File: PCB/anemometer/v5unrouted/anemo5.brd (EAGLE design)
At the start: 100 x 80 mm, 77 parts, among them IC1 AD8223, IC2 AD8223, IC3 AD8223, IC4 AD8223, IC5 TL072D, IC6 TL072D, IC7 TL072D, J1 RJ12STRAIGHT-I2C, J2 RJ12STRAIGHT-I2C

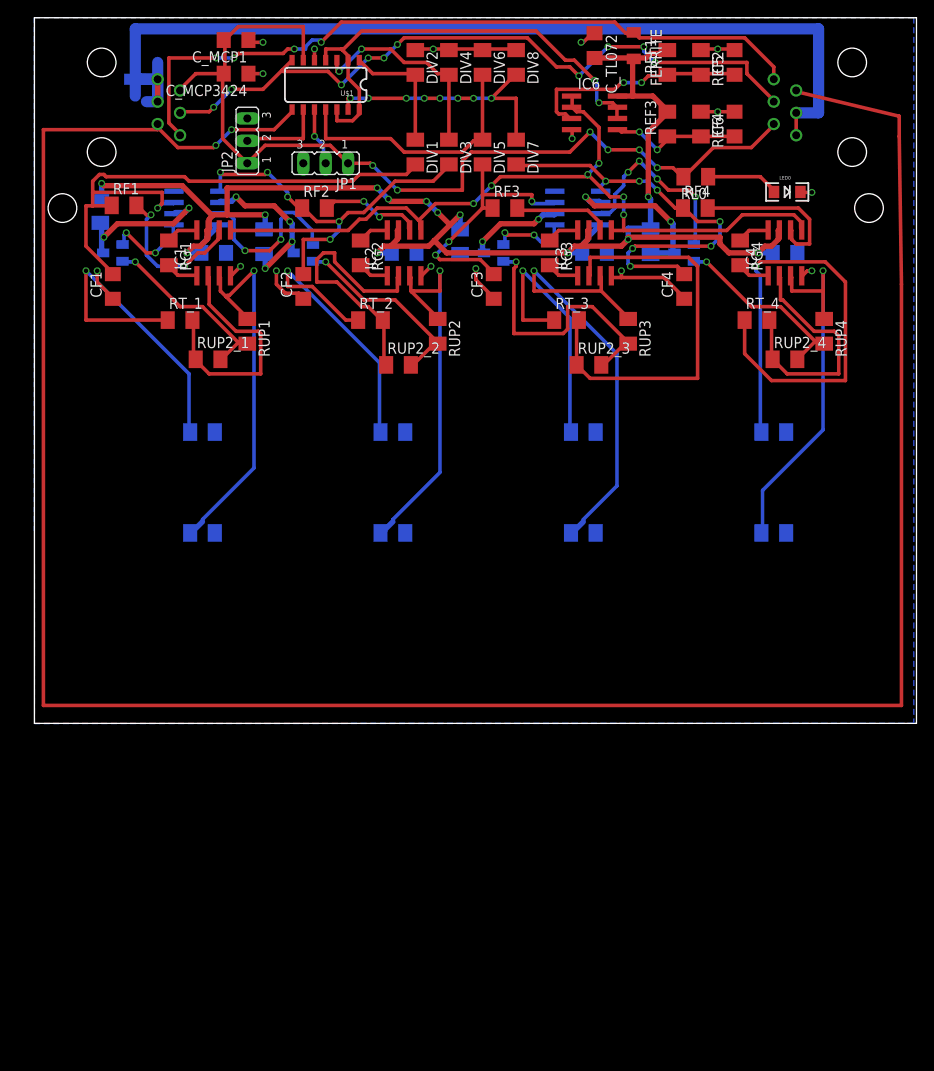
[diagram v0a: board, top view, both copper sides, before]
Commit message: corrected boards to fulfill design rules of the factory in Bogota (drill size and copper spacing. small changes in solardecathlon (SPI pins and design rules changed for zigbee header pads
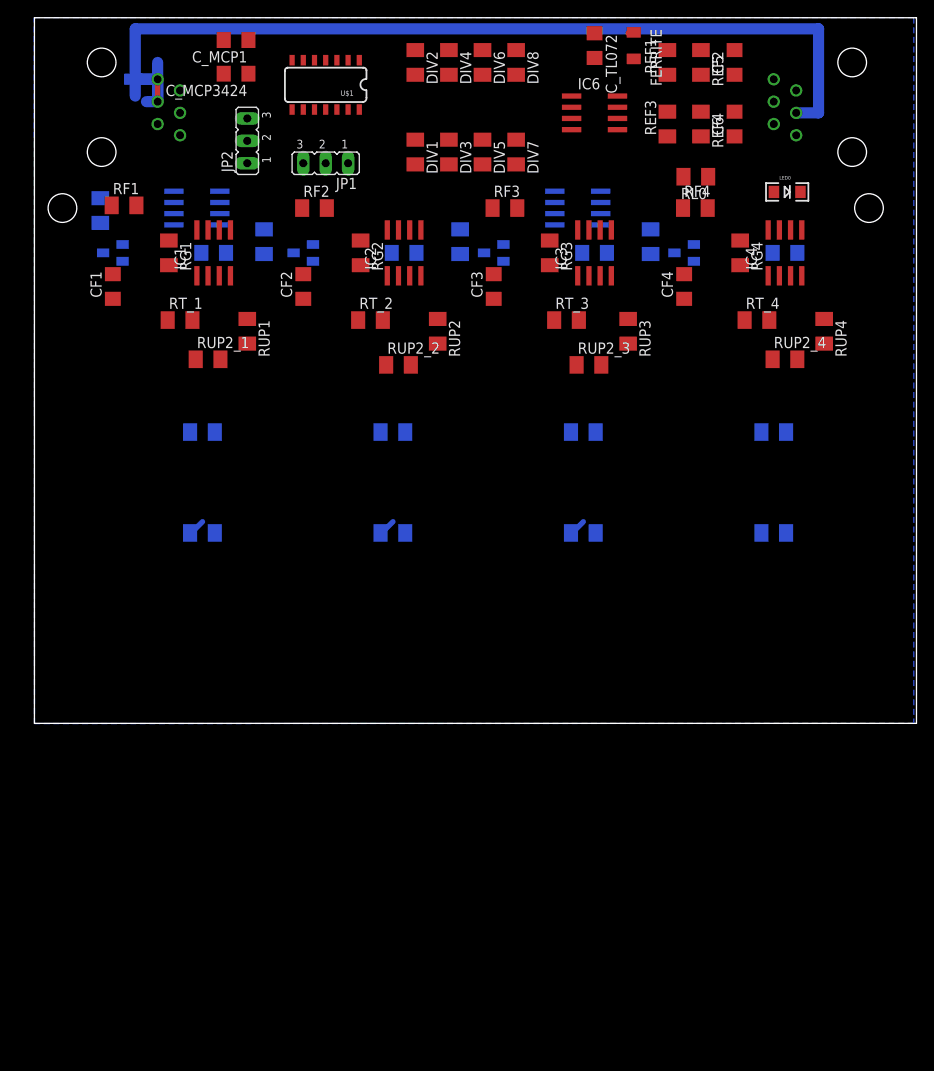
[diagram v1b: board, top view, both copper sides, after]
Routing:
- net SCL: track 273.6 -> 0.00 mm, vias 2 -> 0
- net VCC: track 172.6 -> 0.00 mm, vias 13 -> 0
- net 5V: track 107.3 -> 0.67 mm, vias 6 -> 0
- net REF: track 89.3 -> 0.00 mm, vias 6 -> 0
- net +12V: track 83.6 -> 0.67 mm, vias 4 -> 0
- net SDA: track 80.7 -> 0.00 mm, vias 10 -> 0
- net OUT1: track 64.8 -> 0.00 mm, vias 1 -> 0
- net N$29: track 58.1 -> 0.00 mm, vias 1 -> 0
- net GND: track 67.3 -> 10.4 mm, vias 16 -> 0
- net REF_AD: track 53.5 -> 0.00 mm, vias 2 -> 0
- net IN+3: track 51.9 -> 1.93 mm, vias 1 -> 0
- net OUT4: track 48.3 -> 0.00 mm, vias 7 -> 0
- net IN-3: track 47.2 -> 0.00 mm
- net IN+4: track 43.5 -> 0.13 mm, vias 1 -> 0
- net OUT2: track 43.1 -> 0.00 mm, vias 5 -> 0
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
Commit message: changet to PNP darlington in unrouted anemometer file. should be rerouted if needed! (no changes in routed files...)
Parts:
- moved T4 115.5 mm to (0.00, -35.6), flipped to the top, turned to 0 degrees
- moved T3 94.4 mm to (0.00, -25.4), flipped to the top, turned to 0 degrees
- moved T2 75.0 mm to (0.00, -15.2), flipped to the top, turned to 0 degrees
- moved T1 59.1 mm to (0.00, -5.08), flipped to the top, turned to 0 degrees
- moved LED0 0.78 mm to (86.1, 60.4), flipped to the bottom, turned to 180 degrees
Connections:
- net N$11: now also T2.C; no longer T2.E
- net N$12: now also T3.C; no longer T3.E
- net N$13: now also T4.C; no longer T4.E
- net N$15: now also T1.E; no longer T1.C
- net N$16: now also T2.E; no longer T2.C
- net N$17: now also T3.E; no longer T3.C
- net N$22: now also T4.E; no longer T4.C
- net N$9: now also T1.C; no longer T1.E
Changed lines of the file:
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@@
 <setting verticaltext="up"/>
 </settings>
-<grid distance="200" unitdist="mil" unit="mil" style="lines" multiple="1" display="yes" altdistance="0.025" altunitdist="inch" altunit="inch"/>
+<grid distance="50" unitdist="mil" unit="mil" style="lines" multiple="1" display="yes" altdistance="0.025" altunitdist="inch" altunit="inch"/>
 <layers>
 <layer number="1" name="Top" color="4" fill="1" visible="yes" active="yes"/>
@@
 <element name="CF3" library="rcl" package="C1206" value="330n" x="52.07" y="49.53" rot="R90"/>
 <element name="CF4" library="rcl" package="C1206" value="330n" x="73.66" y="49.53" rot="R90"/>
-<element name="T1" library="transistor" package="SOT23-BEC" value="" x="8.89" y="53.34" rot="MR270"/>
-<element name="T2" library="transistor" package="SOT23-BEC" value="" x="30.48" y="53.34" rot="MR270"/>
-<element name="T3" library="transistor" package="SOT23-BEC" value="" x="52.07" y="53.34" rot="MR270"/>
-<element name="T4" library="transistor" package="SOT23-BEC" value="" x="73.66" y="53.34" rot="MR270"/>
 <element name="J1" library="lpatiny" package="RJ12-STRAIGHT-I2C" value="RJ12STRAIGHT-I2C" x="92.71" y="69.85" rot="MR270"/>
 <element name="DIV1" library="resistor" package="M1206" value="10k" x="43.18" y="64.77" rot="R270"/>
@@
 <element name="J2" library="lpatiny" package="RJ12-STRAIGHT-I2C" value="RJ12STRAIGHT-I2C" x="7.62" y="69.85" rot="MR90"/>
 <element name="RL0" library="resistor" package="M1206" value="1K" x="74.9808" y="61.976" rot="R180"/>
-<element name="LED0" library="SparkFun" package="LED-1206" value="" x="85.344" y="60.2488"/>
+<element name="LED0" library="SparkFun" package="LED-1206" value="" x="86.106" y="60.4012" rot="MR180"/>
 <element name="FERRITE" library="rcl" package="L3216C" value="ferrite" x="67.945" y="76.835" smashed="yes" rot="R270">
 <attribute name="NAME" x="69.85" y="78.74" size="1.27" layer="25" rot="R270"/>
@@
 </element>
 <element name="C6" library="rcl" package="C1206" value="100n" x="79.375" y="67.945" rot="R90"/>
+<element name="T1" library="transistor" package="SOT23-BEC" value="" x="0" y="-5.08"/>
+<element name="T2" library="transistor" package="SOT23-BEC" value="" x="0" y="-15.24"/>
+<element name="T3" library="transistor" package="SOT23-BEC" value="" x="0" y="-25.4"/>
+<element name="T4" library="transistor" package="SOT23-BEC" value="" x="0" y="-35.56"/>
 </elements>
 <signals>
@@
 <contactref element="RUP1" pad="2"/>
 <contactref element="RUP2_1" pad="2"/>
-<contactref element="T1" pad="E"/>
+<contactref element="T1" pad="C"/>
 <wire x1="21.085" y1="41.275" x2="24.13" y2="43.05" width="0" layer="19" extent="1-1"/>
-<wire x1="9.99" y1="52.39" x2="21.085" y2="41.275" width="0" layer="19" extent="1-16"/>
+<wire x1="0" y1="-3.98" x2="21.085" y2="41.275" width="0" layer="19" extent="1-1"/>
 </signal>
 <signal name="N$11">
 <contactref element="RUP2" pad="2"/>
 <contactref element="RUP2_2" pad="2"/>
-<contactref element="T2" pad="E"/>
+<contactref element="T2" pad="C"/>
 <wire x1="42.675" y1="40.64" x2="45.72" y2="43.05" width="0" layer="19" extent="1-1"/>
-<wire x1="31.58" y1="52.39" x2="42.675" y2="40.64" width="0" layer="19" extent="1-16"/>
+<wire x1="0" y1="-14.14" x2="42.675" y2="40.64" width="0" layer="19" extent="1-1"/>
 </signal>
 <signal name="N$12">
 <contactref element="RUP3" pad="2"/>
 <contactref element="RUP2_3" pad="2"/>
-<contactref element="T3" pad="E"/>
+<contactref element="T3" pad="C"/>
 <wire x1="64.265" y1="40.64" x2="67.31" y2="43.05" width="0" layer="19" extent="1-1"/>
-<wire x1="53.17" y1="52.39" x2="64.265" y2="40.64" width="0" layer="19" extent="1-16"/>
+<wire x1="0" y1="-24.3" x2="64.265" y2="40.64" width="0" layer="19" extent="1-1"/>
 </signal>
 <signal name="N$13">
 <contactref element="RUP4" pad="2"/>
 <contactref element="RUP2_4" pad="2"/>
-<contactref element="T4" pad="E"/>
+<contactref element="T4" pad="C"/>
 <wire x1="86.49" y1="41.275" x2="89.535" y2="43.05" width="0" layer="19" extent="1-1"/>
-<wire x1="74.76" y1="52.39" x2="86.49" y2="41.275" width="0" layer="19" extent="1-16"/>
+<wire x1="0" y1="-34.46" x2="86.49" y2="41.275" width="0" layer="19" extent="1-1"/>
 </signal>
 <signal name="N$18">
@@
 <contactref element="RL0" pad="1"/>
 <contactref element="LED0" pad="A"/>
-<wire x1="76.3808" y1="61.976" x2="83.844" y2="60.2488" width="0" layer="19" extent="1-1"/>
+<wire x1="76.3808" y1="61.976" x2="84.606" y2="60.4012" width="0" layer="19" extent="1-1"/>
 </signal>
 <signal name="GND" class="1">
@@
 <wire x1="79.375" y1="69.345" x2="79.375" y2="76.33" width="0" layer="19" extent="1-1"/>
 <wire x1="75.565" y1="69.345" x2="79.375" y2="69.345" width="0" layer="19" extent="1-1"/>
-<wire x1="86.844" y1="60.2488" x2="79.375" y2="69.345" width="0" layer="19" extent="1-1"/>
-<wire x1="86.49" y1="53.34" x2="86.844" y2="60.2488" width="0" layer="19" extent="1-16"/>
+<wire x1="87.606" y1="60.4012" x2="79.375" y2="69.345" width="0" layer="19" extent="1-1"/>
+<wire x1="86.49" y1="53.34" x2="87.606" y2="60.4012" width="0" layer="19" extent="1-16"/>
 <wire x1="86.995" y1="50.74" x2="86.49" y2="53.34" width="0" layer="19" extent="1-16"/>
 <wire x1="63.5" y1="78.235" x2="75.565" y2="76.33" width="0" layer="19" extent="1-1"/>
@@
 </signal>
 <signal name="OUT1A">
-<contactref element="T1" pad="B"/>
 <contactref element="IC5" pad="1"/>
-<wire x1="9.99" y1="54.29" x2="15.815" y2="56.515" width="0" layer="19" extent="16-16"/>
+<contactref element="T1" pad="B"/>
+<wire x1="-0.95" y1="-6.18" x2="15.815" y2="56.515" width="0" layer="19" extent="1-16"/>
 </signal>
 <signal name="OUT2A">
-<contactref element="T2" pad="B"/>
 <contactref element="IC5" pad="7"/>
-<wire x1="21.015" y1="57.785" x2="31.58" y2="54.29" width="0" layer="19" extent="16-16"/>
+<contactref element="T2" pad="B"/>
+<wire x1="-0.95" y1="-16.34" x2="21.015" y2="57.785" width="0" layer="19" extent="1-16"/>
 </signal>
 <signal name="OUT3A">
-<contactref element="T3" pad="B"/>
 <contactref element="IC7" pad="1"/>
-<wire x1="53.17" y1="54.29" x2="58.995" y2="56.515" width="0" layer="19" extent="16-16"/>
+<contactref element="T3" pad="B"/>
+<wire x1="-0.95" y1="-26.5" x2="58.995" y2="56.515" width="0" layer="19" extent="1-16"/>
 </signal>
 <signal name="OUT4A">
-<contactref element="T4" pad="B"/>
 <contactref element="IC7" pad="7"/>
-<wire x1="64.195" y1="57.785" x2="74.76" y2="54.29" width="0" layer="19" extent="16-16"/>
+<contactref element="T4" pad="B"/>
+<wire x1="-0.95" y1="-36.66" x2="64.195" y2="57.785" width="0" layer="19" extent="1-16"/>
 </signal>
 <signal name="N$15" class="2">
-<contactref element="T1" pad="C"/>
 <contactref element="IC5" pad="2"/>
 <contactref element="RC1" pad="1"/>
+<contactref element="T1" pad="E"/>
 <wire x1="7.4676" y1="56.7406" x2="15.815" y2="57.785" width="0" layer="19" extent="16-16"/>
-<wire x1="7.79" y1="53.34" x2="7.4676" y2="56.7406" width="0" layer="19" extent="16-16"/>
+<wire x1="0.95" y1="-6.18" x2="7.4676" y2="56.7406" width="0" layer="19" extent="1-16"/>
 </signal>
 <signal name="N$16" class="2">
-<contactref element="T2" pad="C"/>
 <contactref element="IC5" pad="6"/>
 <contactref element="RC2" pad="1"/>
-<wire x1="26.035" y1="53.21" x2="29.38" y2="53.34" width="0" layer="19" extent="16-16"/>
-<wire x1="21.015" y1="59.055" x2="26.035" y2="53.21" width="0" layer="19" extent="16-16"/>
+<contactref element="T2" pad="E"/>
+<wire x1="26.035" y1="53.21" x2="21.015" y2="59.055" width="0" layer="19" extent="16-16"/>
+<wire x1="0.95" y1="-16.34" x2="26.035" y2="53.21" width="0" layer="19" extent="1-16"/>
 </signal>
 <signal name="N$17" class="2">
-<contactref element="T3" pad="C"/>
 <contactref element="IC7" pad="2"/>
 <contactref element="RC3" pad="1"/>
-<wire x1="50.97" y1="53.34" x2="58.995" y2="57.785" width="0" layer="19" extent="16-16"/>
-<wire x1="48.26" y1="53.21" x2="50.97" y2="53.34" width="0" layer="19" extent="16-16"/>
+<contactref element="T3" pad="E"/>
+<wire x1="48.26" y1="53.21" x2="58.995" y2="57.785" width="0" layer="19" extent="16-16"/>
+<wire x1="0.95" y1="-26.5" x2="48.26" y2="53.21" width="0" layer="19" extent="1-16"/>
 </signal>
 <signal name="N$22" class="2">
-<contactref element="T4" pad="C"/>
 <contactref element="IC7" pad="6"/>
 <contactref element="RC4" pad="1"/>
-<wire x1="69.85" y1="53.21" x2="72.56" y2="53.34" width="0" layer="19" extent="16-16"/>
-<wire x1="64.195" y1="59.055" x2="69.85" y2="53.21" width="0" layer="19" extent="16-16"/>
+<contactref element="T4" pad="E"/>
+<wire x1="69.85" y1="53.21" x2="64.195" y2="59.055" width="0" layer="19" extent="16-16"/>
+<wire x1="0.95" y1="-36.66" x2="69.85" y2="53.21" width="0" layer="19" extent="1-16"/>
 </signal>
 <signal name="REF_AD">
